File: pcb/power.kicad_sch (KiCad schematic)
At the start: 20 parts, among them U1 MIC5335-JGYMT, U2 TPS71918-12DRVR

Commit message: Address OEPS manufacturing concerns
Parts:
- U?: value TPS3839DQN -> TPS3839G18DQNT
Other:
- note added: "NB: V_{thresh} = 1.67V"
- moved on the sheet: C?
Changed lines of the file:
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@@
   (junction (at 96.52 68.58) (diameter 0) (color 0 0 0 0)
   )
-  (junction (at 217.17 113.03) (diameter 0) (color 0 0 0 0)
+  (junction (at 222.25 113.03) (diameter 0) (color 0 0 0 0)
   )
   (junction (at 96.52 121.92) (diameter 0) (color 0 0 0 0)
@@
     (stroke (width 0) (type default))
   )
-  (wire (pts (xy 217.17 113.03) (xy 217.17 115.57))
+  (wire (pts (xy 222.25 113.03) (xy 222.25 115.57))
     (stroke (width 0) (type default))
   )
@@
     (stroke (width 0) (type default))
   )
-  (wire (pts (xy 217.17 111.76) (xy 217.17 113.03))
+  (wire (pts (xy 222.25 111.76) (xy 222.25 113.03))
     (stroke (width 0) (type default))
   )
@@
     (stroke (width 0) (type default))
   )
-  (wire (pts (xy 217.17 113.03) (xy 196.85 113.03))
+  (wire (pts (xy 222.25 113.03) (xy 196.85 113.03))
     (stroke (width 0) (type default))
   )
@@
     (stroke (width 0) (type default))
   )
-  (wire (pts (xy 217.17 127) (xy 217.17 123.19))
+  (wire (pts (xy 222.25 127) (xy 222.25 123.19))
     (stroke (width 0) (type default))
   )
@@
   (wire (pts (xy 140.97 66.04) (xy 142.24 66.04))
     (stroke (width 0) (type default))
+  )
+  (text "NB: V_{thresh} = 1.67V\n" (at 200.66 128.27 0)
+    (effects (font (size 1.27 1.27)) (justify left bottom))
   )
   (text "NB: ~copies IMEC headstage power sequence" (at 97.79 100.33 0)
@@
       (effects (font (size 1.27 1.27)) (justify right))
     )
-    (property "Value" "TPS3839DQN" (at 200.66 123.825 0)
+    (property "Value" "TPS3839G18DQNT" (at 200.66 123.825 0)
       (effects (font (size 1.27 1.27)) (justify right))
     )
@@
     )
   )
-  (symbol (lib_id "power:+1V8") (at 217.17 111.76 0) (unit 1)
-    (in_bom yes) (on_board yes) (dnp no)
-    (property "Reference" "#PWR?" (at 217.17 115.57 0)
-      (effects (font (size 1.27 1.27)) hide)
-    )
-    (property "Value" "+1V8" (at 217.17 107.95 0)
-      (effects (font (size 1.27 1.27)))
-    )
-    (property "Footprint" "" (at 217.17 111.76 0)
-      (effects (font (size 1.27 1.27)) hide)
-    )
-    (property "Datasheet" "" (at 217.17 111.76 0)
+  (symbol (lib_id "power:+1V8") (at 222.25 111.76 0) (unit 1)
+    (in_bom yes) (on_board yes) (dnp no)
+    (property "Reference" "#PWR?" (at 222.25 115.57 0)
+      (effects (font (size 1.27 1.27)) hide)
+    )
+    (property "Value" "+1V8" (at 222.25 107.95 0)
+      (effects (font (size 1.27 1.27)))
+    )
+    (property "Footprint" "" (at 222.25 111.76 0)
+      (effects (font (size 1.27 1.27)) hide)
+    )
+    (property "Datasheet" "" (at 222.25 111.76 0)
       (effects (font (size 1.27 1.27)) hide)
     )
@@
     )
   )
-  (symbol (lib_id "power:GND") (at 217.17 127 0) (mirror y) (unit 1)
-    (in_bom yes) (on_board yes) (dnp no)
-    (property "Reference" "#PWR?" (at 217.17 133.35 0)
-      (effects (font (size 1.27 1.27)) hide)
-    )
-    (property "Value" "GND" (at 217.17 130.81 0)
-      (effects (font (size 1.27 1.27)))
-    )
-    (property "Footprint" "" (at 217.17 127 0)
-      (effects (font (size 1.27 1.27)) hide)
-    )
-    (property "Datasheet" "" (at 217.17 127 0)
+  (symbol (lib_id "power:GND") (at 222.25 127 0) (mirror y) (unit 1)
+    (in_bom yes) (on_board yes) (dnp no)
+    (property "Reference" "#PWR?" (at 222.25 133.35 0)
+      (effects (font (size 1.27 1.27)) hide)
+    )
+    (property "Value" "GND" (at 222.25 130.81 0)
+      (effects (font (size 1.27 1.27)))
+    )
+    (property "Footprint" "" (at 222.25 127 0)
+      (effects (font (size 1.27 1.27)) hide)
+    )
+    (property "Datasheet" "" (at 222.25 127 0)
       (effects (font (size 1.27 1.27)) hide)
     )
@@
     )
   )
-  (symbol (lib_id "Device:C") (at 217.17 119.38 0) (unit 1)
-    (in_bom yes) (on_board yes) (dnp no)
-    (property "Reference" "C?" (at 219.71 118.11 0)
-      (effects (font (size 1.27 1.27)) (justify left))
-    )
-    (property "Value" "0.1uF" (at 219.71 120.65 0)
-      (effects (font (size 1.27 1.27)) (justify left))
-    )
-    (property "Footprint" "Capacitor_SMD:C_0201_0603Metric" (at 218.1352 123.19 0)
-      (effects (font (size 1.27 1.27)) hide)
-    )
-    (property "Datasheet" "~" (at 217.17 119.38 0)
-      (effects (font (size 1.27 1.27)) hide)
-    )
-    (property "TempCo" "X7R" (at 217.17 119.38 0)
-      (effects (font (size 1.27 1.27)) hide)
-    )
-    (property "Voltage" "25V" (at 217.17 119.38 0)
-      (effects (font (size 1.27 1.27)) hide)
-    )
-    (property "CASE/PACKAGE" "0201" (at 217.17 119.38 0)
-      (effects (font (size 1.27 1.27)) hide)
-    )
-    (property "Tolerance" "" (at 217.17 119.38 0)
-      (effects (font (size 1.27 1.27)) hide)
-    )
+  (symbol (lib_id "Device:C") (at 222.25 119.38 0) (unit 1)
+    (in_bom yes) (on_board yes) (dnp no)
+    (property "Reference" "C?" (at 224.79 118.11 0)
+      (effects (font (size 1.27 1.27)) (justify left))
+    )
+    (property "Value" "0.1uF" (at 224.79 120.65 0)
+      (effects (font (size 1.27 1.27)) (justify left))
+    )
+    (property "Footprint" "Capacitor_SMD:C_0201_0603Metric" (at 223.2152 123.19 0)
+      (effects (font (size 1.27 1.27)) hide)
+    )
+    (property "Datasheet" "~" (at 222.25 119.38 0)
+      (effects (font (size 1.27 1.27)) hide)
+    )
+    (property "TempCo" "X7R" (at 222.25 119.38 0)
+      (effects (font (size 1.27 1.27)) hide)
+    )
+    (property "Voltage" "25V" (at 222.25 119.38 0)
+      (effects (font (size 1.27 1.27)) hide)
+    )
+    (property "CASE/PACKAGE" "0201" (at 222.25 119.38 0)
+      (effects (font (size 1.27 1.27)) hide)
+    )
+    (property "Tolerance" "" (at 222.25 119.38 0)
+      (effects (font (size 1.27 1.27)) hide)
+    )

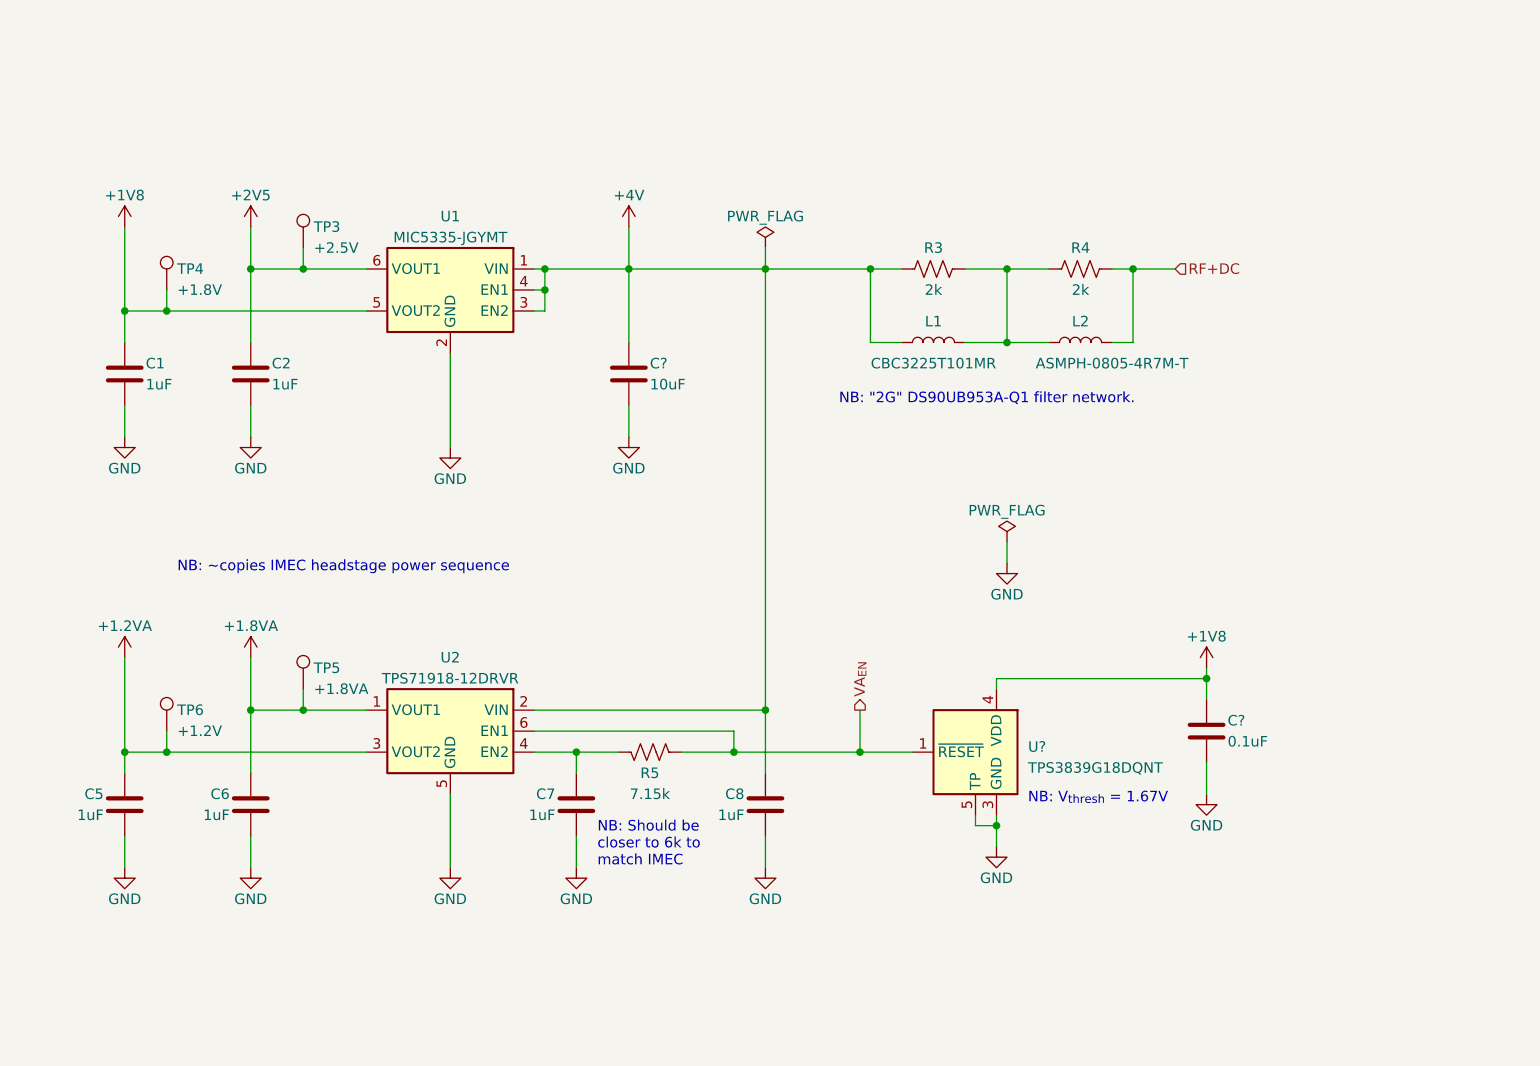
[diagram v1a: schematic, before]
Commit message: Redo NP Power circuit
- For NP 1.0, separate 1.8 and 1.2 rails are needed for digital and
analog sections, respectively, with a delay between power on. This has
been addressed here
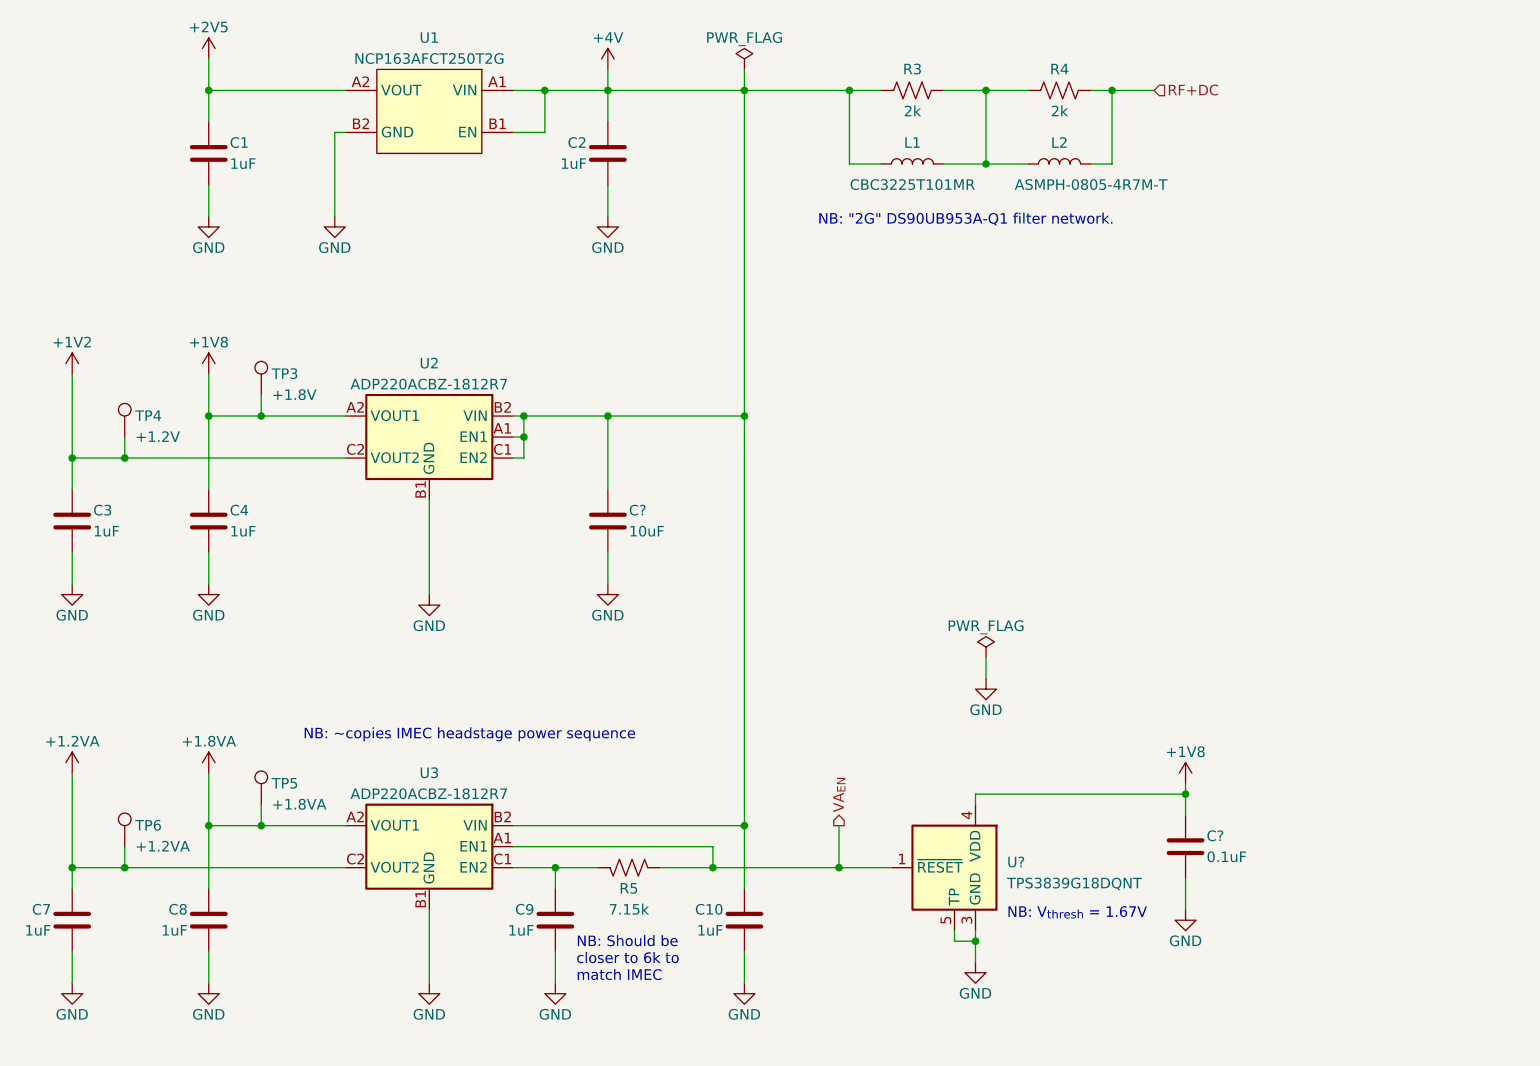
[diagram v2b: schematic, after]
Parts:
- removed U1: MIC5335-JGYMT, jonnew:MICROCHIP_TDFN-6-1EP_1.6x1.6mm_P0.5mm_EP0.5x1.4mm, symbol jonnew:MIC5335-xxxMT
- removed U2: TPS71918-12DRVR, oe_common:TI_DRV0006A_WSON6-2x2x0.75-1x1.6EP, symbol open-ephys:TPS718/9xx
- added C1, C2: 1uF, Capacitor_SMD:C_0201_0603Metric, symbol Device:C
- added U1: NCP163AFCT250T2G, jonnew:ONSEMI_567JZ_WLCSP4-0.64x0.64, symbol jonnew:LDO_EN
- added U2, U3: ADP220ACBZ-1812R7, oe_common:ANALOG_CB-6-2_BGA-6_2x3_1.0x1.45mm, symbol open-ephys:ADP22xXXXX
- TP3: value +2.5V -> +1.8V
- TP4: value +1.8V -> +1.2V
- TP6: value +1.2V -> +1.2VA
- renumbered C8 to C10, C1 to C3, C2 to C4, C5 to C7, C6 to C8, C7 to C9
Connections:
- net +1.2VA: now also U3.C2 (VOUT2)
- net +1.8VA: now also U3.A2 (VOUT1)
- net +1V8: now also C4.1, TP3.1, U2.A2 (VOUT1); no longer C3.1, TP4.1
- net +2V5: now also C1.1, U1.A2 (VOUT); no longer C4.1, TP3.1
- net +4V: now also C2.1, U1.A1 (VIN), U1.B1 (EN), U2.A1 (EN1), U2.B2 (VIN), U2.C1 (EN2), U3.B2 (VIN)
- net GND: now also C1.2, C2.2, U1.B2 (GND), U2.B1 (GND), U3.B1 (GND)
- net VA_{EN}: now also U3.A1 (EN1)
- net at C9.1, R5.2: now also U3.C1 (EN2)
- new net +1V2: C3.1, TP4.1, U2.C2 (VOUT2)
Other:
- moved on the sheet: C10, C3, C4, C7, C8, C9, C?, L1, L2, R3, R4, R5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

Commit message: Revision B
- Tiny changes after testing revision A. Really may not be needed other
than POR chip part number changes (same footprint, different threshold
voltage) and even that is not really needed.
- Fixed mislabelled test point silkscreen
- Added extra 10uF cap to Vcoax
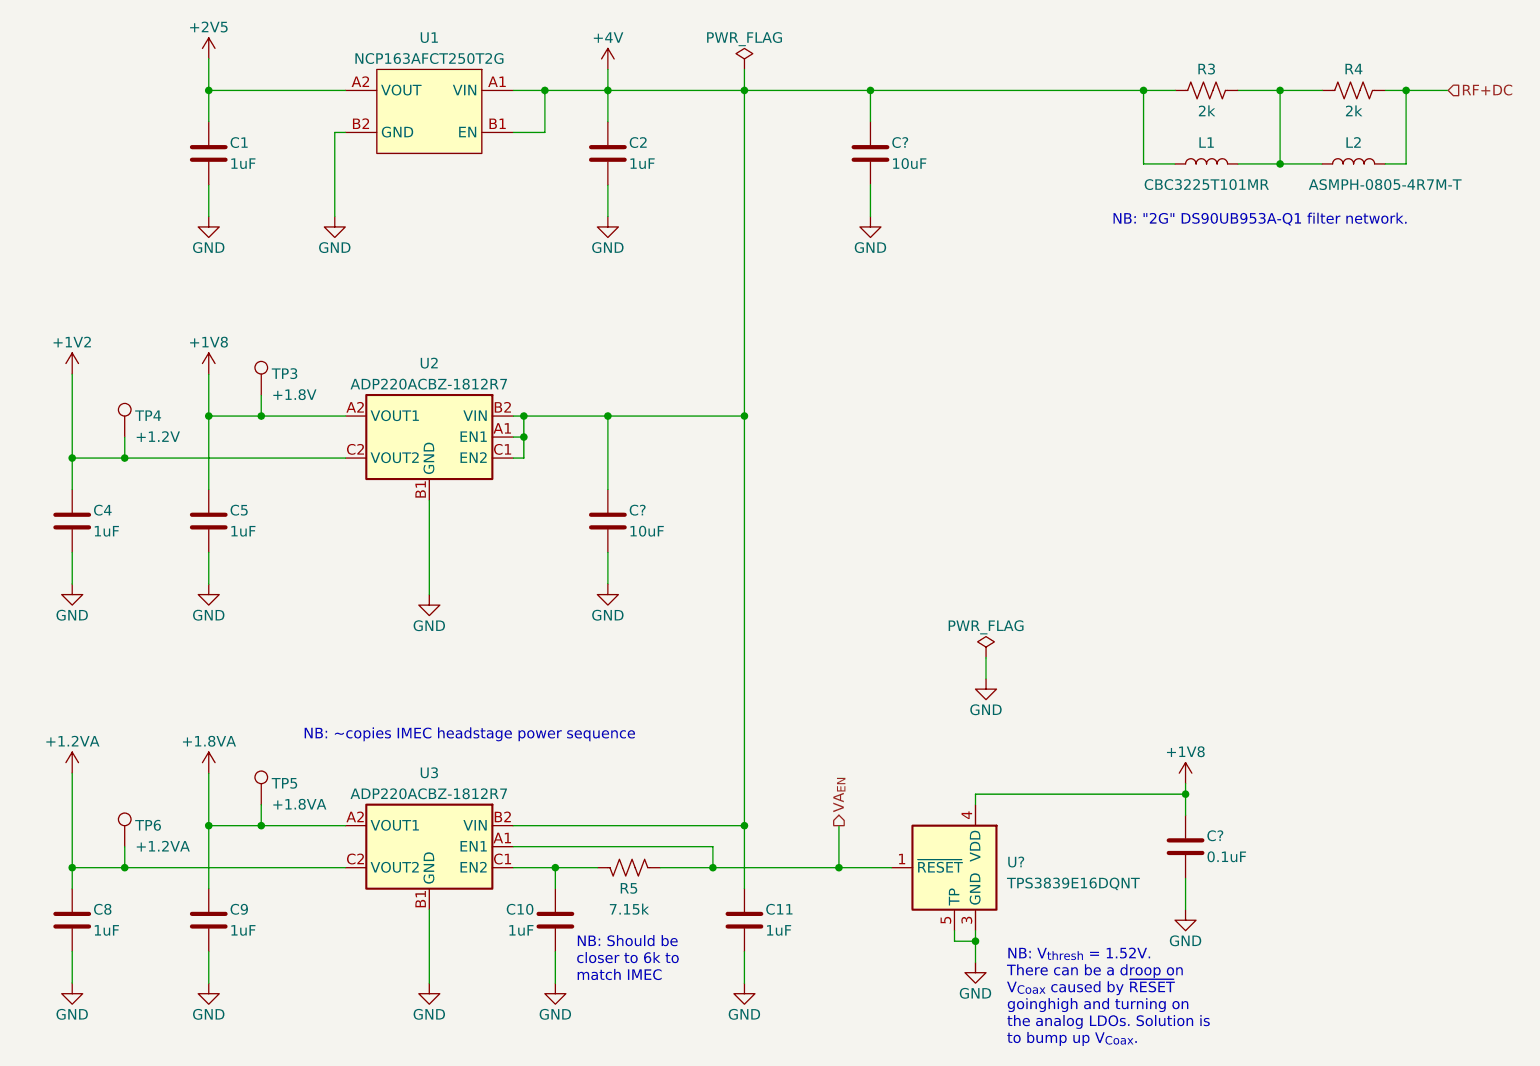
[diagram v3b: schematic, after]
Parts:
- added C?: 10uF, Capacitor_SMD:C_0402_1005Metric, symbol Device:C
- U?: value TPS3839G18DQNT -> TPS3839E16DQNT
- renumbered C9 to C10, C10 to C11, C3 to C4, C4 to C5, C7 to C8, C8 to C9
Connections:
- net +4V: now also C?.1
- net GND: now also C?.2
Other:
- note added: "NB: V_{thresh} = 1.52V. There can be a droop on V_{Coax} caused by ~{RESET} goinghigh and turning on the analog LDOs. Solution is to bump up V_{Coax}."
- note removed: "NB: V_{thresh} = 1.67V"
- moved on the sheet: L1, L2, R3, R4
